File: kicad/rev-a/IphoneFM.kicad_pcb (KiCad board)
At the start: 2 copper layers, 46.5 x 71.4 mm, 106 parts, among them J1 USB 2.0 Type-C, J2 SMA jack, SW1 SPDT, SW2 SPST, SW3 6 × SPST, U1 MCU, U2 Synthesizer, U3 3.3 V 600 mA LDO, U4 FM receiver, U5 SPDT RF switch, U6 USB ESD array, U7 Digital step attenuator, Y2 20 MHz CMOS XO

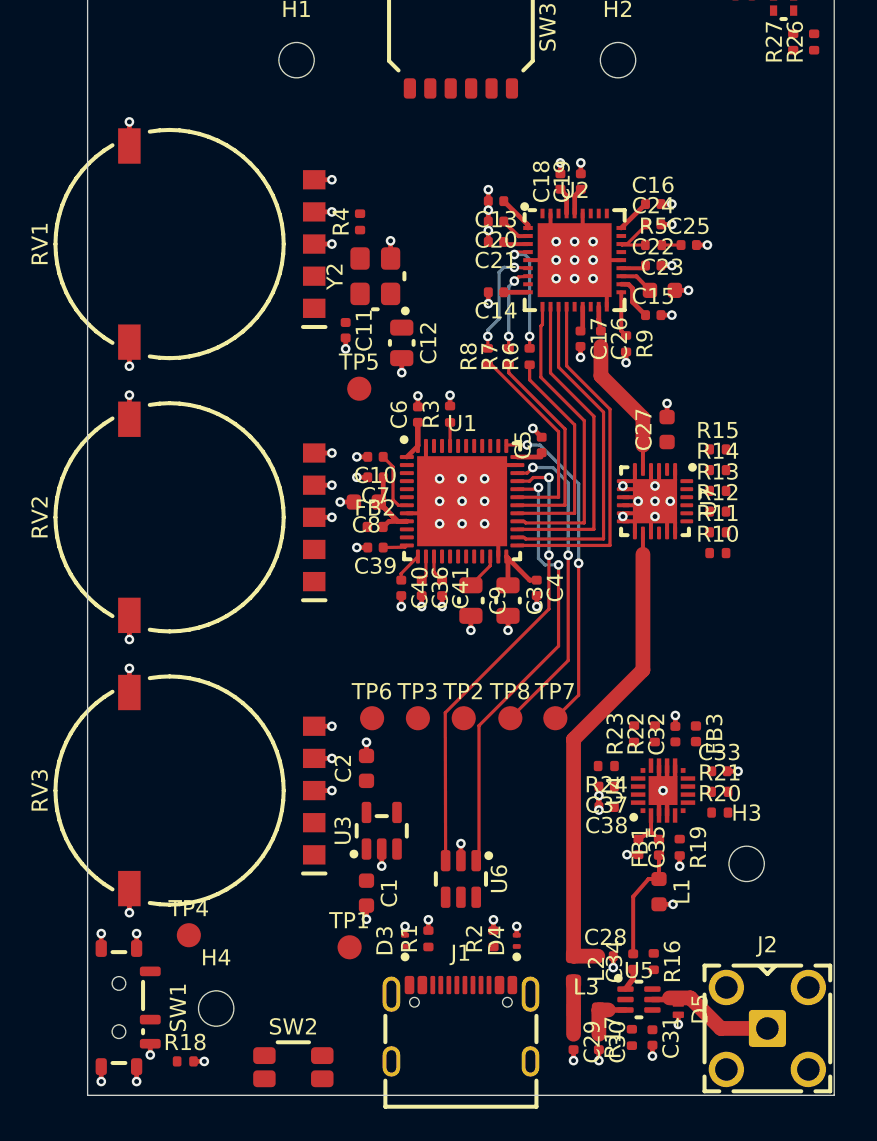
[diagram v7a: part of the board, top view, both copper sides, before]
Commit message: Phase 5: board re-placed to floorplan B3 (U1 turned to face U2/J1 and U4/D1; U2, Y2 and U7 below U1; U4 with its input parts at the top right); routing cleared for a fresh start
Co-Authored-By: Claude Opus 5.5 <noreply@anthropic.com>
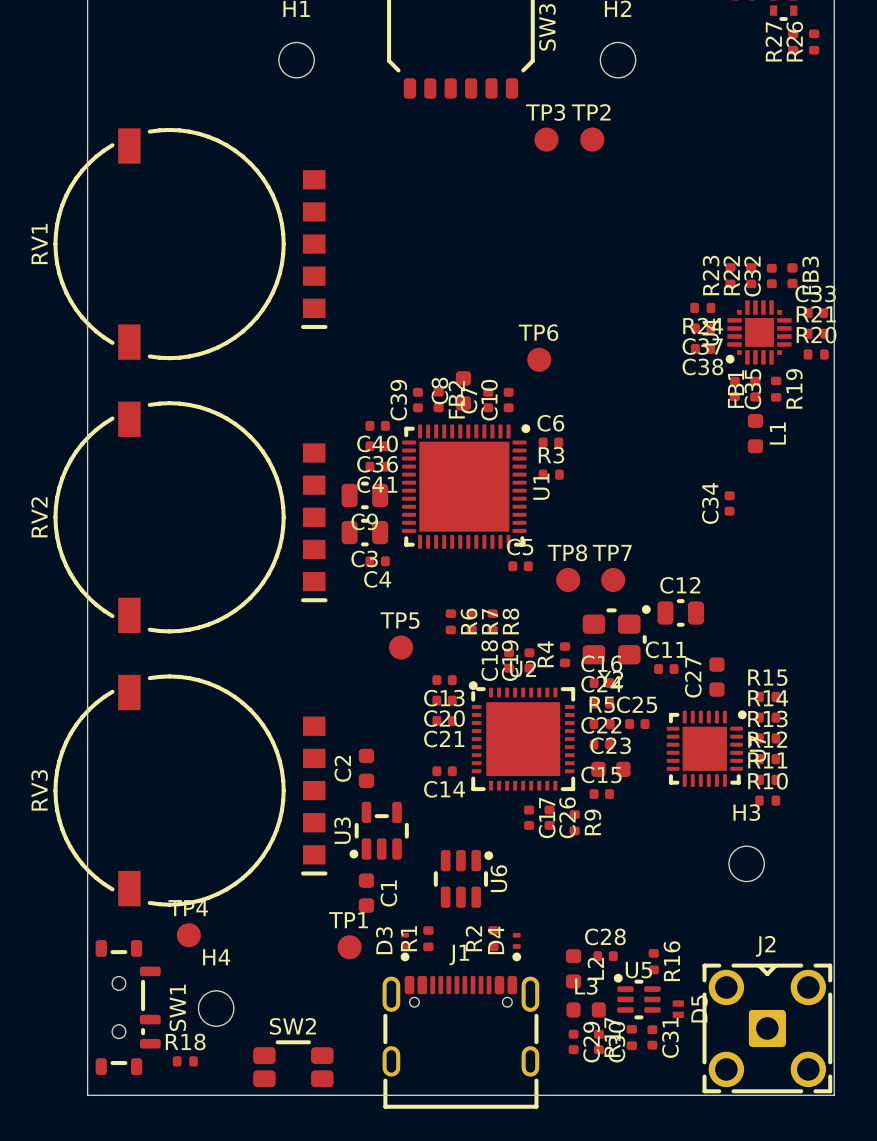
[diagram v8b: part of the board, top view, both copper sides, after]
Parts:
- moved TP2 36.9 mm to (44.1, 71.5)
- moved TP3 36.9 mm to (41.2, 71.5)
- moved C20 30.0 mm to (34.9, 106.4)
- moved C23 30.0 mm to (45.3, 110.7)
- moved C13 30.0 mm to (34.9, 105.1)
- moved C14 30.0 mm to (34.9, 110.8)
- moved C15 30.0 mm to (44.7, 112.2)
- moved C16 30.0 mm to (44.7, 105.3)
- moved C17 30.0 mm to (40.2, 113.7)
- moved C18 30.0 mm to (38.9, 103.9)
- moved C19 30.0 mm to (40.2, 103.9)
- moved C21 30.0 mm to (34.9, 107.7)
- moved C22 30.0 mm to (44.7, 109.1)
- moved C24 30.0 mm to (44.7, 106.6)
- moved C25 30.0 mm to (46.9, 107.9)
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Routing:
- net GND: track 80.8 -> 0.00 mm, vias 98 -> 0
- net /TX_RF_ATT: track 29.6 -> 0.00 mm
- net /USB_DP: track 28.6 -> 0.00 mm, vias 2 -> 0
- net /USB_DM: track 27.7 -> 0.00 mm, vias 2 -> 0
- net 3V3: track 23.3 -> 0.00 mm
- net /LMX_LE: track 21.7 -> 0.00 mm
- net /LMX_DATA: track 21.0 -> 0.00 mm
- net /SWCLK: track 20.8 -> 0.00 mm, vias 2 -> 0
- net /SWDIO: track 19.8 -> 0.00 mm, vias 2 -> 0
- net /LMX_CLK: track 19.7 -> 0.00 mm
- net /LMX_MUX: track 18.8 -> 0.00 mm
- net /FSK_CLK_MCU: track 14.0 -> 0.00 mm
- net /FSK_FS_MCU: track 13.2 -> 0.00 mm
- net /FSK_DATA_MCU: track 12.8 -> 0.00 mm
- net /ATT_IN: track 8.74 -> 0.00 mm
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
